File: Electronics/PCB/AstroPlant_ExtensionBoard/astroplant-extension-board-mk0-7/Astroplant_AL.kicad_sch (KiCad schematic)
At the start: 23 parts, among them J1 JST_XH_Relays, J10 JST_XH_UART, J11 JST_HX_2, J2 2x40 2.5mm Header, J3 JST-XH_3, J4 JST-XH_3, J5 JST_HX_2, J7 JST-XH_3, J8 JST_HX_2, J9 JST-XH_3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

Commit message: Updated PCB from a backup save to solve issue with git
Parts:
- C9: value 100nF -> VJ0603Y104MXJCW1BC
- J1: value JST_XH_Relays -> B6B-XH-A(LF)(SN)
- J10: value JST_XH_UART -> B4B-XH-A(LF)(SN)
- J11, J5, J8: value JST_HX_2 -> B2B-XH-A(LF)(SN)
- J2: value 2x40 2.5mm Header -> 61304021121
- J3, J4, J9: value JST-XH_3 -> B3B-XH-A(LF)(SN)
- J7: value JST-XH_3 -> B3B-XH-A(LF)(SN); MPN B3B-XH-A(LF)(SN) -> B3B-XH-A(LF)(SN)
- R24: value 10k -> CRCW060310K0DHEAP
- SW1, SW2, SW3: value SW_Push -> 430156043726
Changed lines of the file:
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@@
       (effects (font (size 1.524 1.524)))
     )
-    (property "Value" "JST-XH_3" (at 226.06 144.78 90)
+    (property "Value" "B3B-XH-A(LF)(SN) " (at 226.06 144.78 90)
       (effects (font (size 1.524 1.524)))
     )
@@
       (effects (font (size 1.524 1.524)))
     )
-    (property "Value" "JST_XH_UART" (at 57.15 173.99 90)
+    (property "Value" "B4B-XH-A(LF)(SN)" (at 57.15 173.99 90)
       (effects (font (size 1.524 1.524)))
     )
@@
       (effects (font (size 1.524 1.524)))
     )
-    (property "Value" "JST-XH_3" (at 227.33 109.22 90)
+    (property "Value" "B3B-XH-A(LF)(SN) " (at 227.33 109.22 90)
       (effects (font (size 1.524 1.524)))
     )
@@
       (effects (font (size 1.524 1.524)))
     )
-    (property "Value" "JST-XH_3" (at 269.24 143.51 90)
+    (property "Value" "B3B-XH-A(LF)(SN) " (at 269.24 143.51 90)
       (effects (font (size 1.524 1.524)))
     )
@@
       (effects (font (size 1.524 1.524)) hide)
     )
-    (property "MPN" "B3B-XH-A(LF)(SN)" (at 266.7 143.51 0)
+    (property "MPN" "B3B-XH-A(LF)(SN) " (at 266.7 143.51 0)
       (effects (font (size 1.524 1.524)) hide)
     )
@@
       (effects (font (size 1.27 1.27)))
     )
-    (property "Value" "2x40 2.5mm Header" (at 49.53 39.37 0)
+    (property "Value" "61304021121" (at 49.53 39.37 0)
       (effects (font (size 1.27 1.27)))
     )
@@
       (effects (font (size 1.524 1.524)))
     )
-    (property "Value" "JST-XH_3" (at 267.97 107.95 90)
+    (property "Value" "B3B-XH-A(LF)(SN) " (at 267.97 107.95 90)
       (effects (font (size 1.524 1.524)))
     )
@@
       (effects (font (size 1.524 1.524)))
     )
-    (property "Value" "JST_XH_Relays" (at 267.97 38.1 90)
+    (property "Value" "B6B-XH-A(LF)(SN)" (at 267.97 38.1 90)
       (effects (font (size 1.524 1.524)))
     )
@@
       (effects (font (size 1.524 1.524)))
     )
-    (property "Value" "JST_HX_2" (at 127 179.07 0)
+    (property "Value" "B2B-XH-A(LF)(SN) " (at 127 179.07 0)
       (effects (font (size 1.524 1.524)))
     )
@@
       (effects (font (size 1.524 1.524)))
     )
-    (property "Value" "JST_HX_2" (at 128.27 148.59 0)
+    (property "Value" "B2B-XH-A(LF)(SN) " (at 128.27 148.59 0)
       (effects (font (size 1.524 1.524)))
     )
@@
       (effects (font (size 1.27 1.27)) (justify left))
     )
-    (property "Value" "SW_Push" (at 109.22 124.714 0)
+    (property "Value" "430156043726" (at 109.22 124.714 0)
       (effects (font (size 1.27 1.27)))
     )
@@
       (effects (font (size 1.524 1.524)))
     )
-    (property "Value" "JST_HX_2" (at 128.27 120.65 0)
+    (property "Value" "B2B-XH-A(LF)(SN) " (at 128.27 120.65 0)
       (effects (font (size 1.524 1.524)))
     )
@@
       (effects (font (size 1.27 1.27)) (justify right))
     )
-    (property "Value" "10k" (at 133.7972 36.83 0)
+    (property "Value" "CRCW060310K0DHEAP" (at 133.7972 36.83 0)
       (effects (font (size 1.27 1.27)) (justify right))
     )
@@
       (effects (font (size 1.27 1.27)) (justify right))
     )
-    (property "Value" "10k" (at 147.32 60.96 0)
+    (property "Value" "CRCW060310K0DHEAP" (at 147.32 60.96 0)
       (effects (font (size 1.27 1.27)) (justify right))
     )
@@
       (effects (font (size 1.27 1.27)) (justify right))
     )
-    (property "Value" "10k" (at 212.09 101.6 0)
+    (property "Value" "CRCW060310K0DHEAP" (at 212.09 101.6 0)
       (effects (font (size 1.27 1.27)) (justify right))
     )
@@
       (effects (font (size 1.27 1.27)) (justify right))
     )
-    (property "Value" "10k" (at 134.62 60.96 0)
+    (property "Value" "CRCW060310K0DHEAP" (at 134.62 60.96 0)
       (effects (font (size 1.27 1.27)) (justify right))
     )
@@
       (effects (font (size 1.27 1.27)) (justify right))
     )
-    (property "Value" "10k" (at 147.32 36.83 0)
+    (property "Value" "CRCW060310K0DHEAP" (at 147.32 36.83 0)
       (effects (font (size 1.27 1.27)) (justify right))
     )
@@
       (effects (font (size 1.27 1.27)) (justify left))
     )
-    (property "Value" "100nF" (at 22.86 34.2963 0)
+    (property "Value" "VJ0603Y104MXJCW1BC" (at 22.86 34.2963 0)
       (effects (font (size 1.27 1.27)) (justify left))
     )
@@
       (effects (font (size 1.27 1.27)) (justify left))
     )
-    (property "Value" "SW_Push" (at 107.95 183.134 0)
+    (property "Value" "430156043726" (at 107.95 183.134 0)
       (effects (font (size 1.27 1.27)))
     )
@@
       (effects (font (size 1.27 1.27)) (justify left))
     )
-    (property "Value" "100nF" (at 91.44 34.2963 0)
+    (property "Value" "VJ0603Y104MXJCW1BC" (at 91.44 34.2963 0)
       (effects (font (size 1.27 1.27)) (justify left))
     )
@@
       (effects (font (size 1.27 1.27)) (justify left))
     )
-    (property "Value" "SW_Push" (at 109.22 152.654 0)
+    (property "Value" "430156043726" (at 109.22 152.654 0)
       (effects (font (size 1.27 1.27)))
     )
@@
       (effects (font (size 1.27 1.27)) (justify right))
     )
-    (property "Value" "10k" (at 208.28 134.62 0)
+    (property "Value" "CRCW060310K0DHEAP" (at 208.28 134.62 0)
       (effects (font (size 1.27 1.27)) (justify right))
     )

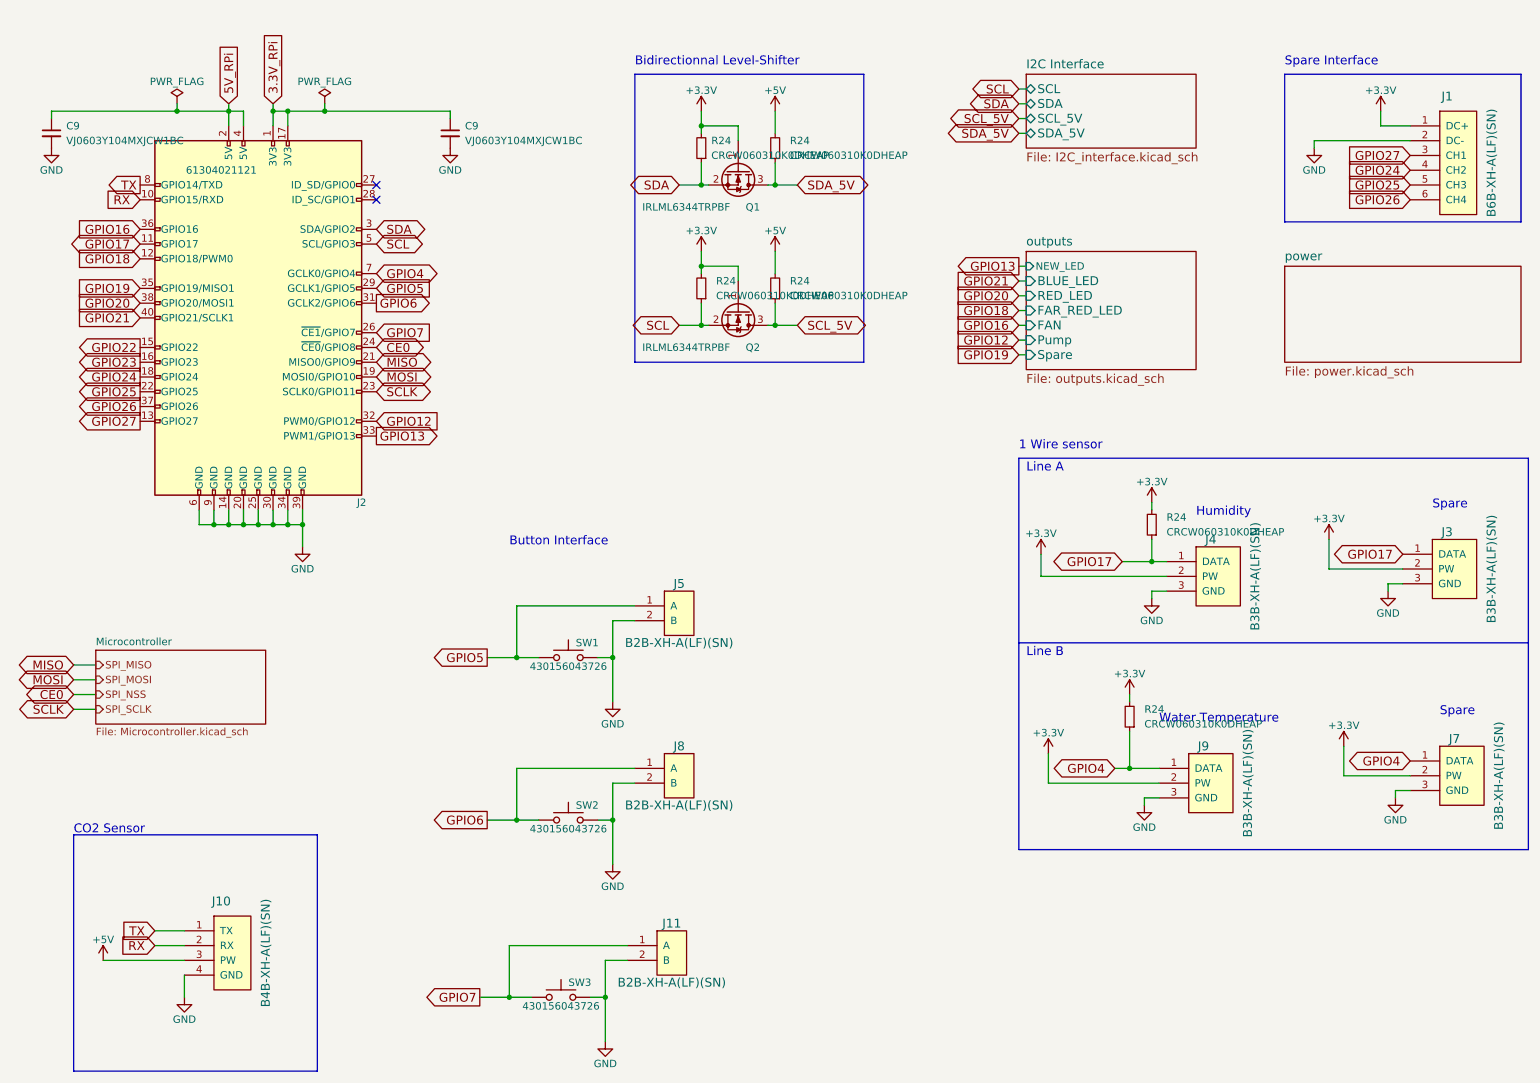
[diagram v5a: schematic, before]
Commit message: Last commit (software + hardware change)
hardware : updated readme, change pcb to solve the issues of the 1st prototype
software : add code (to create a zigbee network)
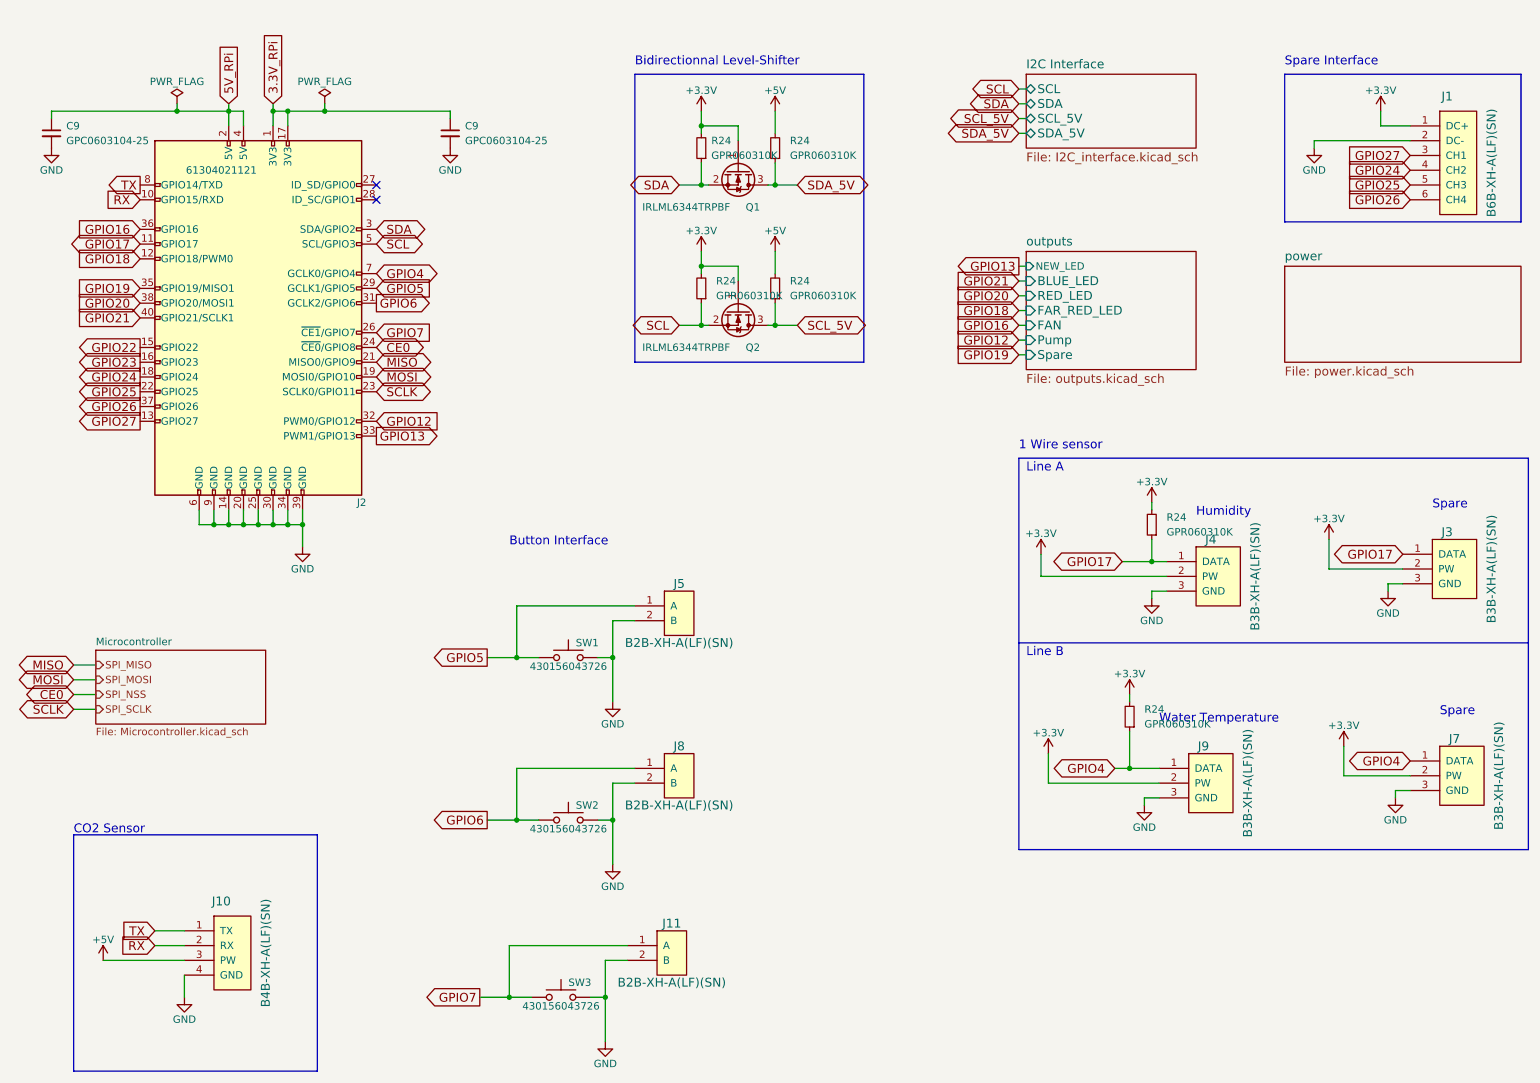
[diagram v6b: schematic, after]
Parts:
- C9: value VJ0603Y104MXJCW1BC -> GPC0603104-25; Capacitance (none) -> 100nF; MPN VJ0603Y104MXJCW1BC -> GPC0603104-25
- R24: value CRCW060310K0DHEAP -> GPR060310K; MPN CRCW060310K0DHEAP -> GPR060310K
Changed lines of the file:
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@@
       (effects (font (size 1.27 1.27)) (justify right))
     )
-    (property "Value" "CRCW060310K0DHEAP" (at 133.7972 36.83 0)
+    (property "Value" "GPR060310K" (at 133.7972 36.83 0)
       (effects (font (size 1.27 1.27)) (justify right))
     )
@@
       (effects (font (size 1.27 1.27)) hide)
     )
-    (property "MPN" "CRCW060310K0DHEAP" (at 132.08 35.56 0)
+    (property "MPN" "GPR060310K" (at 132.08 35.56 0)
       (effects (font (size 1.27 1.27)) hide)
     )
@@
       (effects (font (size 1.27 1.27)) (justify right))
     )
-    (property "Value" "CRCW060310K0DHEAP" (at 147.32 60.96 0)
+    (property "Value" "GPR060310K" (at 147.32 60.96 0)
       (effects (font (size 1.27 1.27)) (justify right))
     )
@@
       (effects (font (size 1.27 1.27)) hide)
     )
-    (property "MPN" "CRCW060310K0DHEAP" (at 144.78 59.69 0)
+    (property "MPN" "GPR060310K" (at 144.78 59.69 0)
       (effects (font (size 1.27 1.27)) hide)
     )
@@
       (effects (font (size 1.27 1.27)) (justify right))
     )
-    (property "Value" "CRCW060310K0DHEAP" (at 212.09 101.6 0)
+    (property "Value" "GPR060310K" (at 212.09 101.6 0)
       (effects (font (size 1.27 1.27)) (justify right))
     )
@@
       (effects (font (size 1.27 1.27)) hide)
     )
-    (property "MPN" "CRCW060310K0DHEAP" (at 209.55 100.33 0)
+    (property "MPN" "GPR060310K" (at 209.55 100.33 0)
       (effects (font (size 1.27 1.27)) hide)
     )
@@
       (effects (font (size 1.27 1.27)) (justify right))
     )
-    (property "Value" "CRCW060310K0DHEAP" (at 134.62 60.96 0)
+    (property "Value" "GPR060310K" (at 134.62 60.96 0)
       (effects (font (size 1.27 1.27)) (justify right))
     )
@@
       (effects (font (size 1.27 1.27)) hide)
     )
-    (property "MPN" "CRCW060310K0DHEAP" (at 132.08 59.69 0)
+    (property "MPN" "GPR060310K" (at 132.08 59.69 0)
       (effects (font (size 1.27 1.27)) hide)
     )
@@
       (effects (font (size 1.27 1.27)) (justify right))
     )
-    (property "Value" "CRCW060310K0DHEAP" (at 147.32 36.83 0)
+    (property "Value" "GPR060310K" (at 147.32 36.83 0)
       (effects (font (size 1.27 1.27)) (justify right))
     )
@@
       (effects (font (size 1.27 1.27)) hide)
     )
-    (property "MPN" "CRCW060310K0DHEAP" (at 144.78 35.56 0)
+    (property "MPN" "GPR060310K" (at 144.78 35.56 0)
       (effects (font (size 1.27 1.27)) hide)
     )
@@
       (effects (font (size 1.27 1.27)) (justify left))
     )
-    (property "Value" "VJ0603Y104MXJCW1BC" (at 22.86 34.2963 0)
+    (property "Value" "GPC0603104-25 " (at 22.86 34.2963 0)
       (effects (font (size 1.27 1.27)) (justify left))
     )
@@
       (effects (font (size 1.27 1.27)) hide)
     )
-    (property "MPN" "VJ0603Y104MXJCW1BC" (at 20.32 33.02 0)
+    (property "MPN" "GPC0603104-25 " (at 20.32 33.02 0)
+      (effects (font (size 1.27 1.27)) hide)
+    )
+    (property "Capacitance" "100nF" (at 20.32 33.02 0)
       (effects (font (size 1.27 1.27)) hide)
     )
@@
       (effects (font (size 1.27 1.27)) (justify left))
     )
-    (property "Value" "VJ0603Y104MXJCW1BC" (at 91.44 34.2963 0)
+    (property "Value" "GPC0603104-25 " (at 91.44 34.2963 0)
       (effects (font (size 1.27 1.27)) (justify left))
     )
@@
       (effects (font (size 1.27 1.27)) hide)
     )
-    (property "MPN" "VJ0603Y104MXJCW1BC" (at 88.9 33.02 0)
+    (property "MPN" "GPC0603104-25 " (at 88.9 33.02 0)
+      (effects (font (size 1.27 1.27)) hide)
+    )
+    (property "Capacitance" "100nF" (at 88.9 33.02 0)
       (effects (font (size 1.27 1.27)) hide)
     )
@@
       (effects (font (size 1.27 1.27)) (justify right))
     )
-    (property "Value" "CRCW060310K0DHEAP" (at 208.28 134.62 0)
+    (property "Value" "GPR060310K" (at 208.28 134.62 0)
       (effects (font (size 1.27 1.27)) (justify right))
     )
@@
       (effects (font (size 1.27 1.27)) hide)
     )
-    (property "MPN" "CRCW060310K0DHEAP" (at 205.74 133.35 0)
-      (effects (font (size 1.27 1.27)) hide)
-    )
+    (property "MPN" "GPR060310K" (at 205.74 133.35 0)
+      (effects (font (size 1.27 1.27)) hide)
+    )
